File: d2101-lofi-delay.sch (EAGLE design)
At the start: 84 parts, among them U1 FX2-20P-1.27DS, U2 FX2-20S-1.27DS

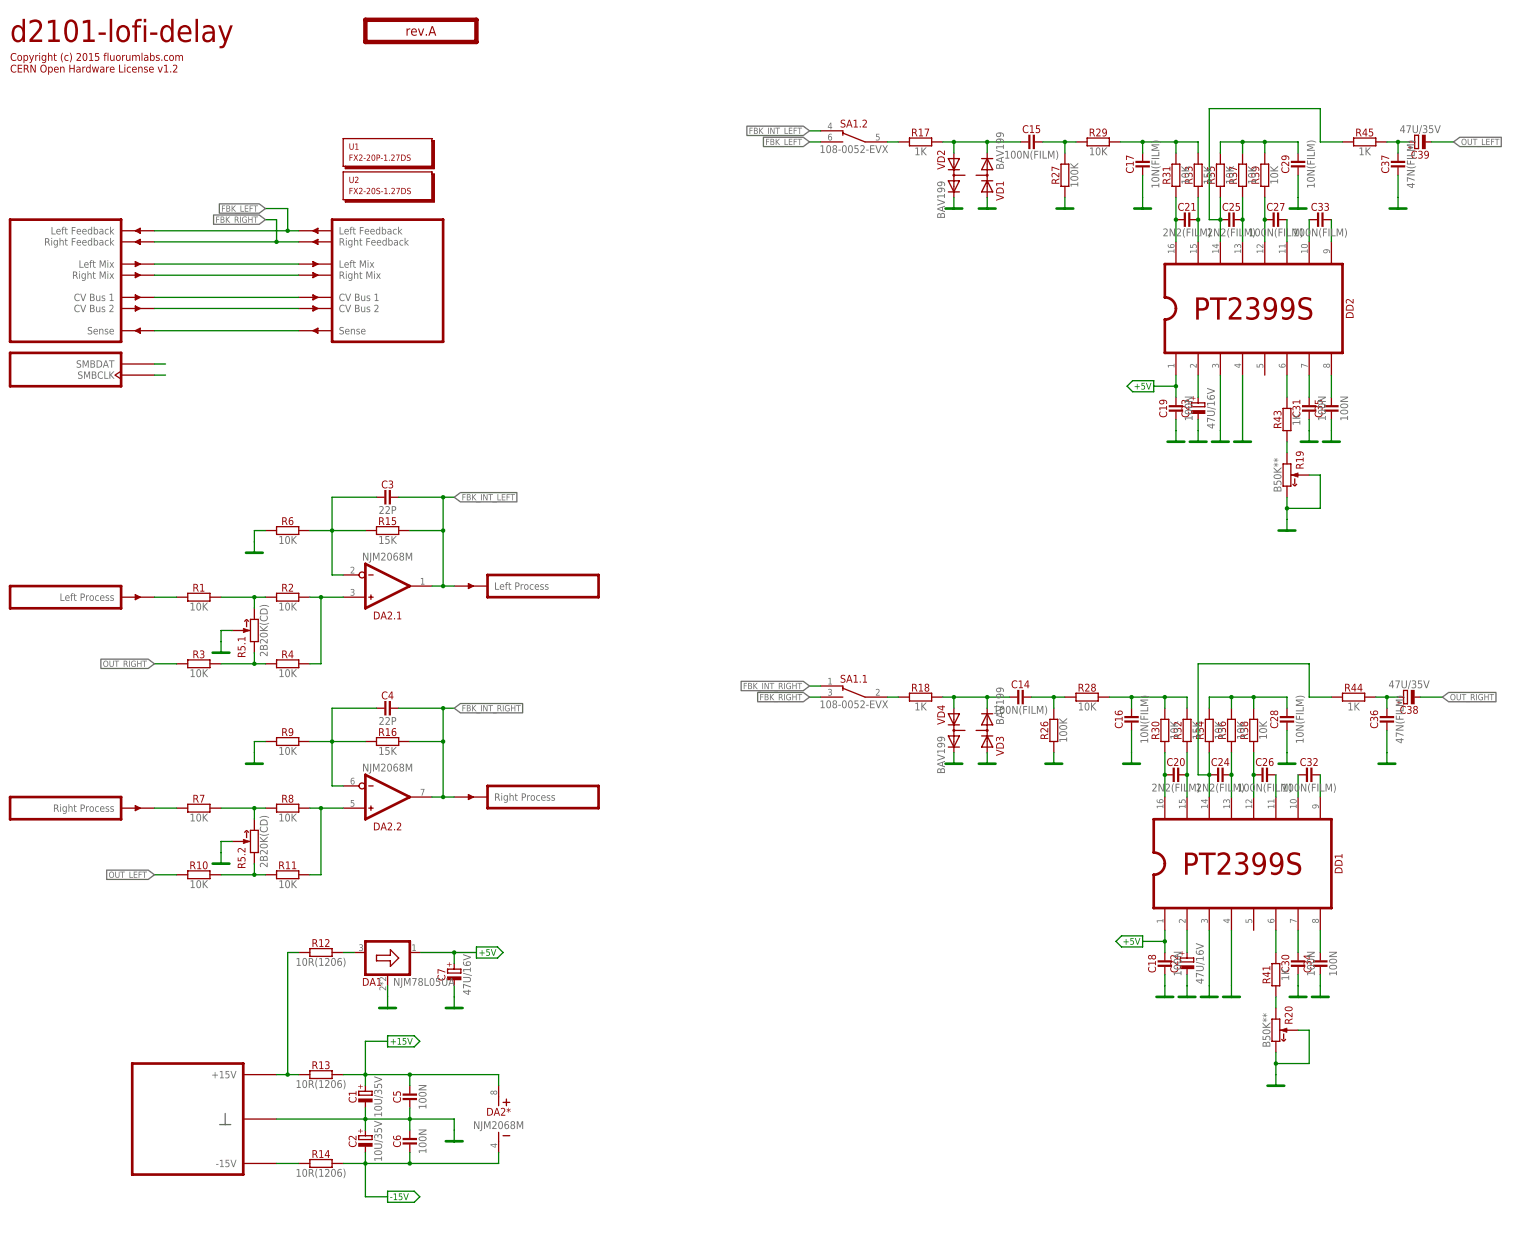
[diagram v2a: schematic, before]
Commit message: Replace 10R with ferrite bead Replace 47u/35V with 33u/25V
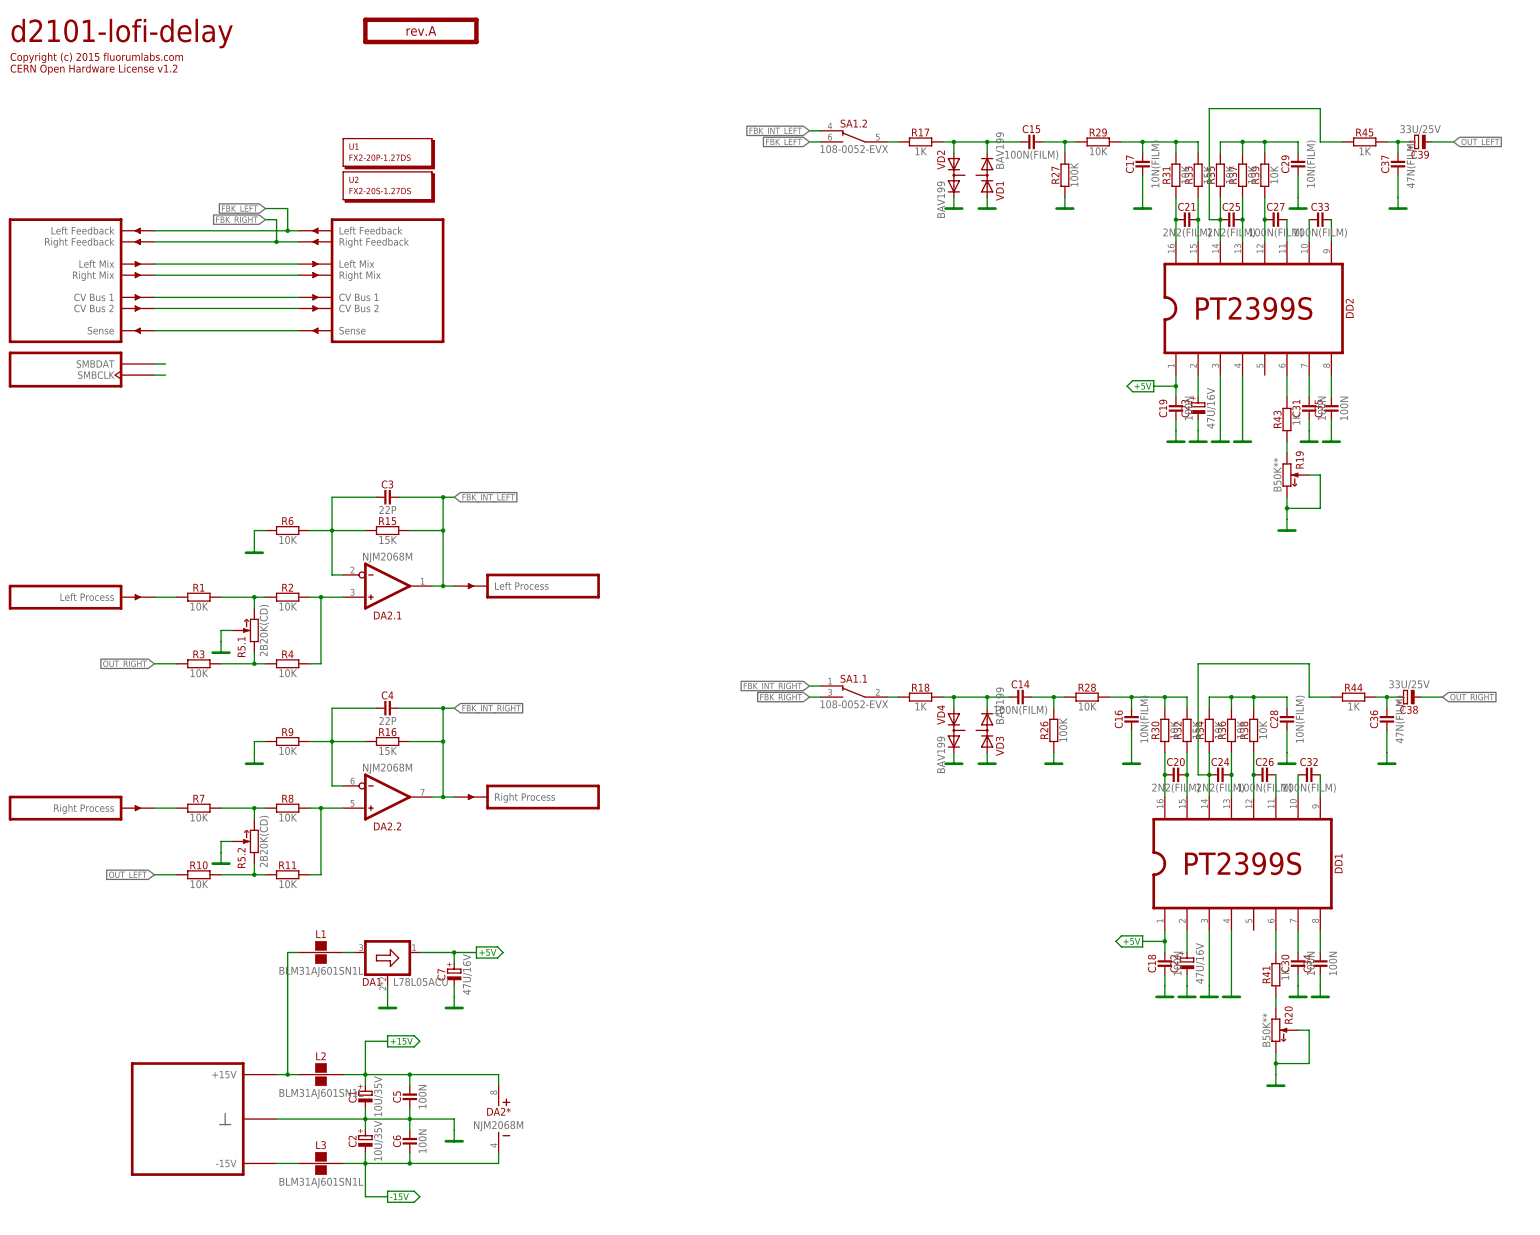
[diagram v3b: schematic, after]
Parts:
- removed R12, R13, R14: 10R(1206), resistors:10R(1206)
- added L1, L2, L3: BLM31AJ601SN1L, inductors:BLM31AJ601SN1L
- C38, C39: value 47U/35V -> 33U/25V; device capacitors-electrolytic:47U/35V -> capacitors-electrolytic:33U/25V
- DA1: value NJM78L05UA -> L78L05ACU; device regulators-linear:NJM78L05UA -> regulators-linear:L78L05ACU
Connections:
- net +15V: now also L2.2; no longer R13.2
- net -15V: now also L3.2; no longer R14.2
- net N$36: now also L3.1; no longer R14.1
- net N$44: now also L1.2; no longer R12.2
- net P+15V: now also L1.1, L2.1; no longer R12.1, R13.1
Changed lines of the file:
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@@
 <part name="PWR3" library="f-supply" deviceset="+5V" device=""/>
 <part name="PWR5" library="f-supply" deviceset="+5V" device=""/>
-<part name="DA1" library="regulators-linear" deviceset="?" device="NJM78L05UA" value="NJM78L05UA"/>
-<part name="R13" library="resistors" deviceset="?" device="10R(1206)"/>
-<part name="R12" library="resistors" deviceset="?" device="10R(1206)"/>
-<part name="R14" library="resistors" deviceset="?" device="10R(1206)"/>
+<part name="DA1" library="regulators-linear" deviceset="?" device="L78L05ACU" value="L78L05ACU"/>
+<part name="L2" library="inductors" deviceset="BLM31AJ601SN1L" device=""/>
+<part name="L1" library="inductors" deviceset="BLM31AJ601SN1L" device=""/>
+<part name="L3" library="inductors" deviceset="BLM31AJ601SN1L" device=""/>
 <part name="GND7" library="supply" deviceset="GND" device=""/>
 <part name="C1" library="capacitors-electrolytic" deviceset="?" device="10U/35V"/>
@@
 <part name="R45" library="resistors" deviceset="?" device="1K"/>
 <part name="C37" library="capacitors" deviceset="?" device="47N(FILM)"/>
-<part name="C39" library="capacitors-electrolytic" deviceset="?" device="47U/35V"/>
+<part name="C39" library="capacitors-electrolytic" deviceset="?" device="33U/25V" value="33U/25V"/>
 <part name="GND15" library="supply" deviceset="GND" device=""/>
 <part name="GND27" library="supply" deviceset="GND" device=""/>
@@
 <part name="R44" library="resistors" deviceset="?" device="1K"/>
 <part name="C36" library="capacitors" deviceset="?" device="47N(FILM)"/>
-<part name="C38" library="capacitors-electrolytic" deviceset="?" device="47U/35V"/>
+<part name="C38" library="capacitors-electrolytic" deviceset="?" device="33U/25V" value="33U/25V"/>
 <part name="GND25" library="supply" deviceset="GND" device=""/>
 <part name="GND14" library="supply" deviceset="GND" device=""/>
@@
 <instance part="PWR5" gate="G$1" x="284.48" y="-40.64" rot="R90"/>
 <instance part="DA1" gate="G$1" x="109.22" y="-170.18"/>
-<instance part="R13" gate="G$1" x="93.98" y="-198.12"/>
-<instance part="R12" gate="G$1" x="93.98" y="-170.18"/>
-<instance part="R14" gate="G$1" x="93.98" y="-218.44"/>
+<instance part="L2" gate="G$1" x="93.98" y="-198.12"/>
+<instance part="L1" gate="G$1" x="93.98" y="-170.18"/>
+<instance part="L3" gate="G$1" x="93.98" y="-218.44"/>
 <instance part="GND7" gate="VR1" x="124.46" y="-213.36"/>
 <instance part="C1" gate="G$1" x="104.14" y="-203.2" rot="R270"/>
@@
 <wire x1="86.36" y1="-198.12" x2="86.36" y2="-170.18" width="0.1524" layer="91"/>
 <wire x1="86.36" y1="-170.18" x2="88.9" y2="-170.18" width="0.1524" layer="91"/>
-<pinref part="R13" gate="G$1" pin="1"/>
-<pinref part="R12" gate="G$1" pin="1"/>
+<pinref part="L2" gate="G$1" pin="1"/>
+<pinref part="L1" gate="G$1" pin="1"/>
 <wire x1="83.82" y1="-198.12" x2="86.36" y2="-198.12" width="0.1524" layer="91"/>
 <junction x="86.36" y="-198.12"/>
@@
 <junction x="114.3" y="-198.12"/>
 <wire x1="134.62" y1="-200.66" x2="134.62" y2="-198.12" width="0.1524" layer="91"/>
-<pinref part="R13" gate="G$1" pin="2"/>
+<pinref part="L2" gate="G$1" pin="2"/>
 <pinref part="C1" gate="G$1" pin="+"/>
 <pinref part="C5" gate="G$1" pin="2"/>
@@
 <wire x1="114.3" y1="-215.9" x2="114.3" y2="-218.44" width="0.1524" layer="91"/>
 <junction x="114.3" y="-218.44"/>
-<pinref part="R14" gate="G$1" pin="2"/>
+<pinref part="L3" gate="G$1" pin="2"/>
 <pinref part="C2" gate="G$1" pin="-"/>
 <pinref part="C6" gate="G$1" pin="1"/>
@@
 <wire x1="101.6" y1="-170.18" x2="99.06" y2="-170.18" width="0.1524" layer="91"/>
 <pinref part="DA1" gate="G$1" pin="IN"/>
-<pinref part="R12" gate="G$1" pin="2"/>
+<pinref part="L1" gate="G$1" pin="2"/>
 </segment>
 </net>
@@
 <net name="N$36" class="0">
 <segment>
-<pinref part="R14" gate="G$1" pin="1"/>
+<pinref part="L3" gate="G$1" pin="1"/>
 <wire x1="83.82" y1="-218.44" x2="88.9" y2="-218.44" width="0.1524" layer="91"/>
 <pinref part="PCB1" gate="G$9" pin="P-15V"/>

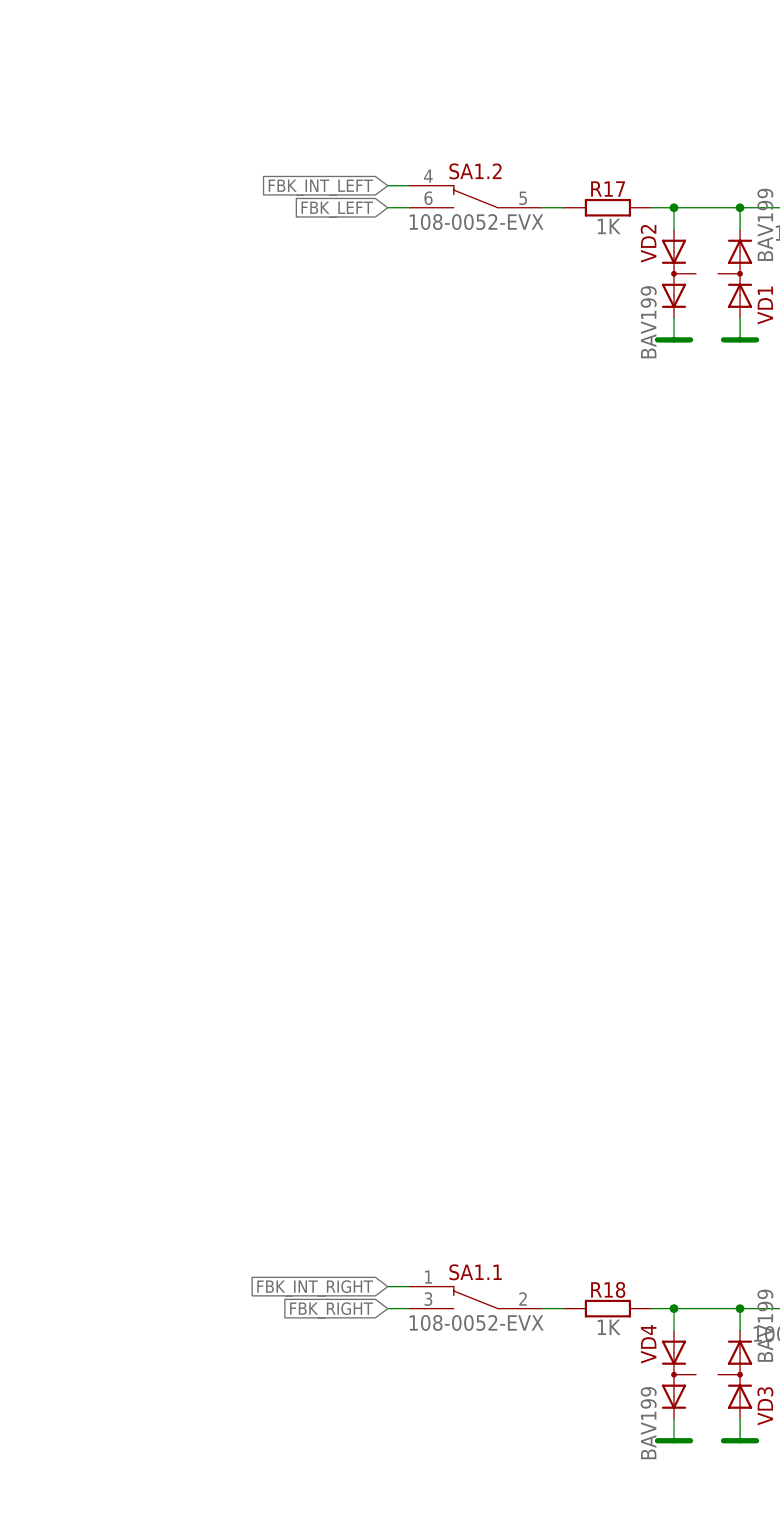
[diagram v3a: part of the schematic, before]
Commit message: Replace feedback switch with MJS22R
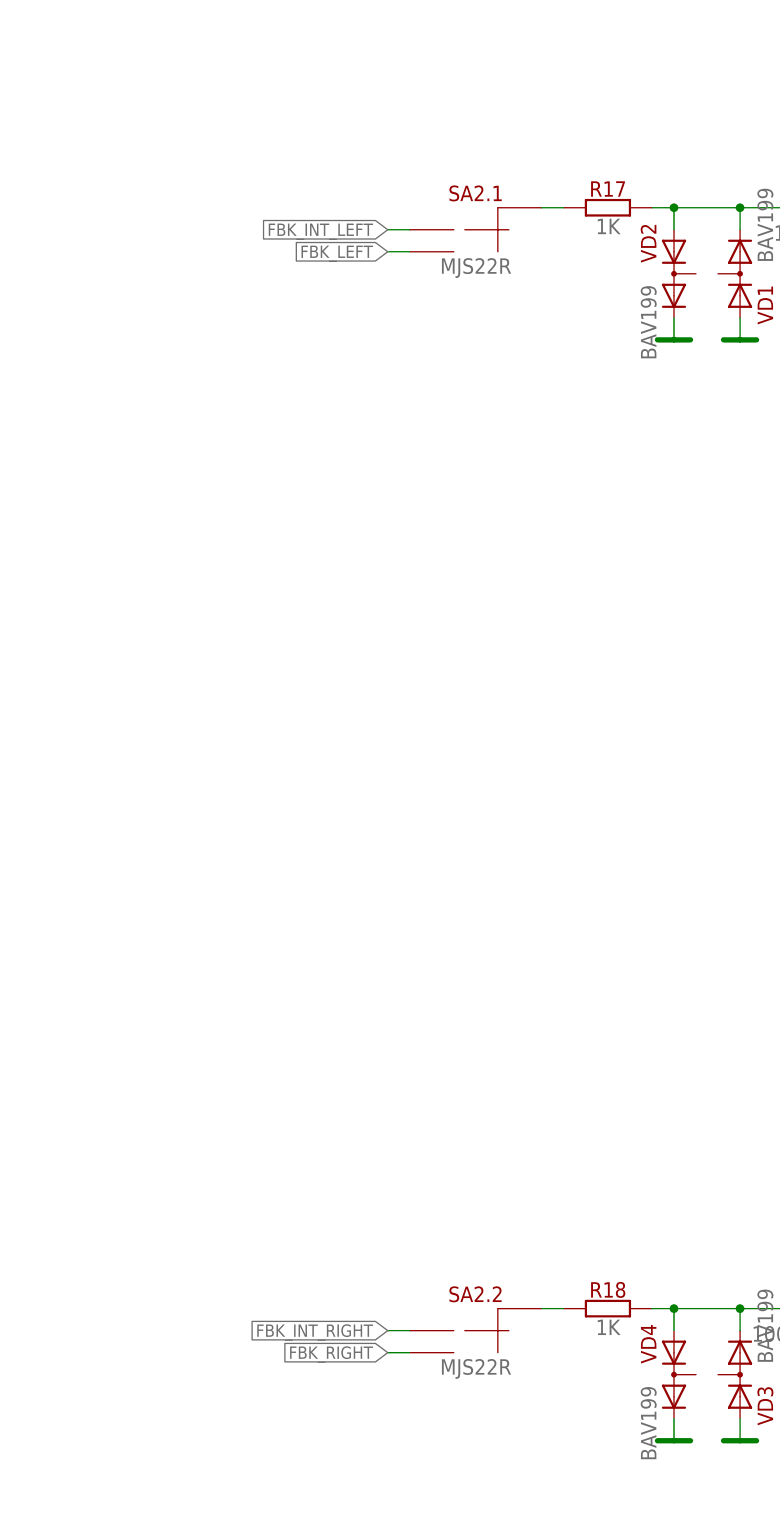
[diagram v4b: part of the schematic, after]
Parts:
- removed SA1: 108-0052-EVX, switches:108-0052-EVX
- added SA2: MJS22R, switches:MJS22R
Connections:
- net FBK_INT_LEFT: now also SA2.1.1; no longer SA1.2.NC
- net FBK_INT_RIGHT: now also SA2.2.1; no longer SA1.1.NC
- net FBK_LEFT: now also SA2.1.2; no longer SA1.2.NO
- net FBK_RIGHT: now also SA2.2.2; no longer SA1.1.NO
- net N$13: now also SA2.2.CM; no longer SA1.1.CM
- net N$6: now also SA2.1.CM; no longer SA1.2.CM
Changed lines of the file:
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@@
 <part name="R26" library="resistors" deviceset="?" device="100K"/>
 <part name="GND12" library="supply" deviceset="GND" device=""/>
-<part name="SA1" library="switches" deviceset="108-0052-EVX" device=""/>
 <part name="R9" library="resistors" deviceset="?" device="10K"/>
 <part name="R16" library="resistors" deviceset="?" device="15K"/>
@@
 <part name="R20" library="potentiometers" deviceset="?" device="B50K**"/>
 <part name="GND24" library="supply" deviceset="GND" device=""/>
+<part name="SA2" library="switches" deviceset="MJS22R" device=""/>
 </parts>
 <sheets>
@@
 <instance part="R26" gate="G$1" x="261.62" y="-119.38" rot="R90"/>
 <instance part="GND12" gate="VR1" x="261.62" y="-127"/>
-<instance part="SA1" gate=".1" x="215.9" y="-111.76" rot="MR0"/>
 <instance part="R9" gate="G$1" x="86.36" y="-121.92"/>
 <instance part="R16" gate="G$1" x="109.22" y="-121.92"/>
@@
 <instance part="PCB1" gate="G$5" x="144.78" y="-134.62"/>
 <instance part="PCB1" gate="G$9" x="63.5" y="-208.28"/>
-<instance part="SA1" gate=".2" x="215.9" y="15.24" rot="MR0"/>
 <instance part="VD1" gate="G$1" x="246.38" y="7.62" rot="R90"/>
 <instance part="VD2" gate="G$1" x="238.76" y="7.62" rot="R270"/>
@@
 <instance part="R20" gate="G$1" x="312.42" y="-187.96" rot="R270"/>
 <instance part="GND24" gate="VR1" x="312.42" y="-200.66"/>
+<instance part="SA2" gate=".1" x="215.9" y="12.7" rot="MR0"/>
+<instance part="SA2" gate=".2" x="215.9" y="-114.3" rot="MR0"/>
 </instances>
 <busses>
@@
 </segment>
 <segment>
-<pinref part="SA1" gate=".1" pin="NO"/>
-<wire x1="208.28" y1="-111.76" x2="205.74" y2="-111.76" width="0.1524" layer="91"/>
-<label x="205.74" y="-111.76" size="1.4224" layer="95" rot="R180" xref="yes"/>
+<label x="205.74" y="-116.84" size="1.4224" layer="95" rot="R180" xref="yes"/>
+<pinref part="SA2" gate=".2" pin="2"/>
+<wire x1="208.28" y1="-116.84" x2="205.74" y2="-116.84" width="0.1524" layer="91"/>
 </segment>
 </net>
@@
 </segment>
 <segment>
-<pinref part="SA1" gate=".2" pin="NO"/>
-<wire x1="208.28" y1="15.24" x2="205.74" y2="15.24" width="0.1524" layer="91"/>
-<label x="205.74" y="15.24" size="1.4224" layer="95" rot="R180" xref="yes"/>
+<label x="205.74" y="10.16" size="1.4224" layer="95" rot="R180" xref="yes"/>
+<pinref part="SA2" gate=".1" pin="2"/>
+<wire x1="208.28" y1="10.16" x2="205.74" y2="10.16" width="0.1524" layer="91"/>
 </segment>
 </net>
@@
 </segment>
 <segment>
-<pinref part="SA1" gate=".2" pin="NC"/>
-<wire x1="208.28" y1="17.78" x2="205.74" y2="17.78" width="0.1524" layer="91"/>
-<label x="205.74" y="17.78" size="1.4224" layer="95" rot="R180" xref="yes"/>
+<label x="205.74" y="12.7" size="1.4224" layer="95" rot="R180" xref="yes"/>
+<pinref part="SA2" gate=".1" pin="1"/>
+<wire x1="208.28" y1="12.7" x2="205.74" y2="12.7" width="0.1524" layer="91"/>
 </segment>
 </net>
@@
 </segment>
 <segment>
-<pinref part="SA1" gate=".1" pin="NC"/>
-<wire x1="208.28" y1="-109.22" x2="205.74" y2="-109.22" width="0.1524" layer="91"/>
-<label x="205.74" y="-109.22" size="1.4224" layer="95" rot="R180" xref="yes"/>
+<label x="205.74" y="-114.3" size="1.4224" layer="95" rot="R180" xref="yes"/>
+<pinref part="SA2" gate=".2" pin="1"/>
+<wire x1="208.28" y1="-114.3" x2="205.74" y2="-114.3" width="0.1524" layer="91"/>
 </segment>
 </net>
@@
 <net name="N$6" class="0">
 <segment>
-<pinref part="SA1" gate=".2" pin="CM"/>
 <pinref part="R17" gate="G$1" pin="1"/>
 <wire x1="223.52" y1="15.24" x2="226.06" y2="15.24" width="0.1524" layer="91"/>
+<pinref part="SA2" gate=".1" pin="CM"/>
 </segment>
 </net>
 <net name="N$13" class="0">
 <segment>
-<pinref part="SA1" gate=".1" pin="CM"/>
 <pinref part="R18" gate="G$1" pin="1"/>
 <wire x1="223.52" y1="-111.76" x2="226.06" y2="-111.76" width="0.1524" layer="91"/>
-</segment>
-</net>
+<pinref part="SA2" gate=".2" pin="CM"/>
+</segment>
+</net>
